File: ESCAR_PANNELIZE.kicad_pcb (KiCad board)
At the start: 2 copper layers, 96.6 x 63.6 mm, 168 parts, among them P1 MICRO_SD, P2 BREADBOARD, P3 PROGRAM, P4 MOTOR_B, P5 MOTOR_A, P6 CONN_01X10, P7 CONN_01X10, P8 POWER_IN, P9 UNIVERSAL_PAD, SW1 RESET, SW2 MULTIFUNCTION_SW, SW3 POWER_SW, U1 ESP-WROOM-02, U2 TC117HS, U3 TC117HS, U4 LD1117CV33

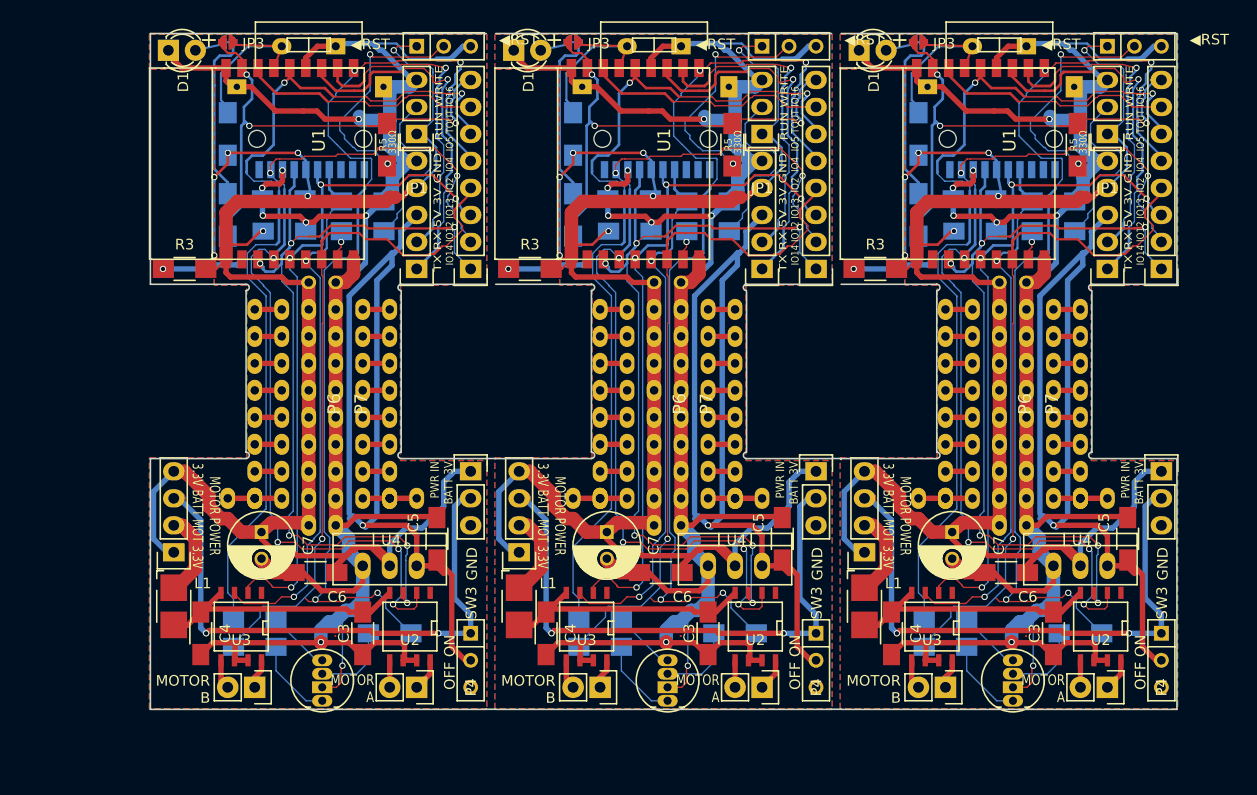
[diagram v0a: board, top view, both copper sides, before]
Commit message: add dividing resisters for RX pin , and organized many point.
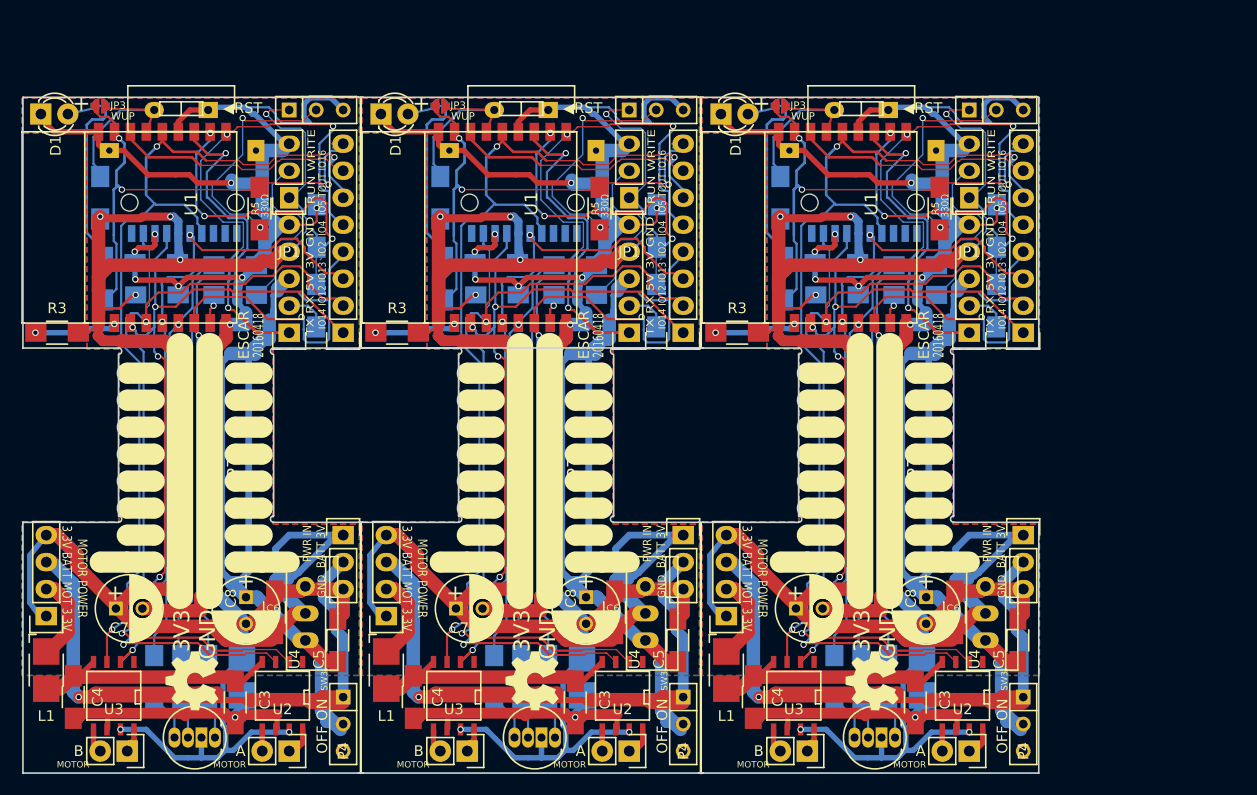
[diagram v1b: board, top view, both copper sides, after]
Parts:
- removed the C1 at (144.5, 67.1)
- removed the C1 at (112.0, 67.1)
- removed the C1 at (177.0, 67.1)
- removed the C2 at (144.5, 70.1)
- removed the C2 at (112.0, 70.1)
- removed the C2 at (177.0, 70.1)
- removed the C3 at (151.9, 108.0)
- removed the C3 at (119.4, 108.0)
- removed the C3 at (184.4, 108.0)
- removed the C4 at (136.6, 108.0)
- removed the C4 at (104.1, 108.0)
- removed the C4 at (169.1, 108.0)
- removed the C5 at (158.9, 99.1)
- removed the C5 at (126.4, 99.1)
- removed the C5 at (191.4, 99.1)
- removed the C6 at (147.4, 102.2)
- removed the C6 at (114.9, 102.2)
- removed the C6 at (179.9, 102.2)
- removed the C7 at (142.4, 98.4)
- removed the C7 at (109.9, 98.4)
- removed the C7 at (174.9, 98.4)
- removed the D1 at (133.6, 53.1)
- removed the D1 at (101.1, 53.1)
- removed the D1 at (166.1, 53.1)
- removed the D2 at (148.1, 114.3)
- removed the D2 at (115.6, 114.3)
- removed the D2 at (180.6, 114.3)
- removed the JP1 at (157.0, 61.0)
- removed the JP1 at (124.5, 61.0)
- removed the JP1 at (189.5, 61.0)
- removed the JP2 at (139.2, 52.3)
- removed the JP2 at (106.7, 52.3)
- removed the JP2 at (171.7, 52.3)
- removed the JP3 at (139.2, 52.3)
- removed the JP3 at (106.7, 52.3)
- removed the JP3 at (171.7, 52.3)
- removed the JP4 at (134.1, 100.3)
- removed the JP4 at (101.6, 100.3)
- removed the JP4 at (166.6, 100.3)
- removed the L1 at (134.1, 105.4)
- removed the L1 at (101.6, 105.4)
- removed the L1 at (166.6, 105.4)
- removed the P1 at (147.4, 58.4)
- removed the P1 at (114.9, 58.4)
- removed the P1 at (179.9, 58.4)
- removed the P2 at (162.0, 73.7)
- removed the P2 at (129.5, 73.7)
- removed the P2 at (194.5, 73.7)
- removed the P3 at (157.0, 73.7)
- removed the P3 at (124.5, 73.7)
- removed the P3 at (189.5, 73.7)
- removed the P4 at (157.0, 113.0)
- removed the P4 at (124.5, 113.0)
- removed the P4 at (189.5, 113.0)
- removed the P5 at (141.7, 113.0)
- removed the P5 at (109.2, 113.0)
- removed the P5 at (174.2, 113.0)
- removed the P6 at (146.8, 86.4)
- removed the P6 at (114.3, 86.4)
- removed the P6 at (179.3, 86.4)
- removed the P7 at (149.3, 86.4)
- removed the P7 at (116.8, 86.4)
- removed the P7 at (181.8, 86.4)
- removed the P8 at (162.0, 92.7)
- removed the P8 at (129.5, 92.7)
- removed the P8 at (194.5, 92.7)
- removed the P9 at (140.4, 95.2)
- removed the P9 at (153.2, 82.5)
- removed the P9 at (143.0, 82.5)
- removed the P9 at (143.0, 85.1)
- removed the P9 at (143.0, 80.0)
- removed the P9 at (143.0, 77.5)
- removed the P9 at (143.0, 87.6)
- removed the P9 at (143.0, 90.2)
- removed the P9 at (143.0, 95.2)
- removed the P9 at (143.0, 92.7)
- removed the P9 at (108.0, 95.2)
- removed the P9 at (155.7, 95.2)
- removed the P9 at (123.2, 95.2)
- removed the P9 at (120.7, 92.7)
- removed the P9 at (120.7, 95.2)
- removed the P9 at (120.7, 90.2)
- removed the P9 at (120.7, 87.6)
- removed the P9 at (120.7, 77.5)
- removed the P9 at (120.7, 80.0)
- removed the P9 at (120.7, 85.1)
- removed the P9 at (120.7, 82.5)
- removed the P9 at (110.5, 82.5)
- removed the P9 at (153.2, 92.7)
- removed the P9 at (110.5, 85.1)
- removed the P9 at (110.5, 80.0)
- removed the P9 at (110.5, 77.5)
- removed the P9 at (110.5, 87.6)
- removed the P9 at (110.5, 90.2)
- removed the P9 at (110.5, 95.2)
- removed the P9 at (110.5, 92.7)
- removed the P9 at (172.9, 95.2)
- removed the P9 at (188.2, 95.2)
- removed the P9 at (185.7, 92.7)
- removed the P9 at (153.2, 95.2)
- removed the P9 at (185.7, 95.2)
- removed the P9 at (185.7, 90.2)
- removed the P9 at (185.7, 87.6)
- removed the P9 at (185.7, 77.5)
- removed the P9 at (185.7, 80.0)
- removed the P9 at (185.7, 85.1)
- removed the P9 at (185.7, 82.5)
- removed the P9 at (175.5, 82.5)
- removed the P9 at (175.5, 85.1)
- removed the P9 at (175.5, 80.0)
- removed the P9 at (153.2, 90.2)
- removed the P9 at (175.5, 77.5)
- removed the P9 at (175.5, 87.6)
- removed the P9 at (175.5, 90.2)
- removed the P9 at (175.5, 95.2)
- removed the P9 at (175.5, 92.7)
- removed the P9 at (153.2, 87.6)
- removed the P9 at (153.2, 77.5)
- removed the P9 at (153.2, 80.0)
- removed the P9 at (153.2, 85.1)
- removed the R1 at (151.9, 67.3)
- removed the R1 at (119.4, 67.3)
- removed the R1 at (184.4, 67.3)
- removed the R2 at (151.9, 70.1)
- removed the R2 at (119.4, 70.1)
- removed the R2 at (184.4, 70.1)
- removed the R3 at (135.1, 73.7)
- removed the R3 at (102.6, 73.7)
- removed the R3 at (167.6, 73.7)
- removed the R4 at (139.2, 61.0)
- removed the R4 at (106.7, 61.0)
- removed the R4 at (171.7, 61.0)
- removed the R5 at (154.2, 62.0)
- removed the R5 at (121.7, 62.0)
- removed the R5 at (186.7, 62.0)
- removed the R6 at (139.2, 68.6)
- removed the R6 at (106.7, 68.6)
- removed the R6 at (171.7, 68.6)
- removed the R7 at (154.4, 108.0)
- removed the R7 at (121.9, 108.0)
- removed the R7 at (186.9, 108.0)
- removed the R8 at (141.7, 106.7)
- removed the R8 at (109.2, 106.7)
- removed the R8 at (174.2, 106.7)
- removed the R9 at (141.7, 109.2)
- removed the R9 at (109.2, 109.2)
- removed the R9 at (174.2, 109.2)
- removed the SW1 at (150.6, 52.6)
- removed the SW1 at (118.1, 52.6)
- removed the SW1 at (183.1, 52.6)
- removed the SW2 at (159.5, 52.7)
- removed the SW2 at (127.0, 52.7)
- removed the SW2 at (192.0, 52.7)
- removed the SW3 at (162.0, 110.5)
- removed the SW3 at (129.5, 110.5)
- removed the SW3 at (194.5, 110.5)
- removed the U1 at (145.0, 63.8)
- removed the U1 at (112.5, 63.8)
- removed the U1 at (177.5, 63.8)
- removed the U2 at (156.3, 107.3)
- removed the U2 at (123.8, 107.3)
- removed the U2 at (188.8, 107.3)
- removed the U3 at (140.4, 107.3)
- removed the U3 at (108.0, 107.3)
- removed the U3 at (172.9, 107.3)
- removed the U4 at (154.4, 101.6)
- removed the U4 at (121.9, 101.6)
- removed the U4 at (186.9, 101.6)
- added C1: 0.1uF, Capacitors_SMD:C_1206_HandSoldering, B.Cu at (100.0, 73.1)
- added C1: 0.1uF, Capacitors_SMD:C_1206_HandSoldering, B.Cu at (132.0, 73.1)
- added C1: 0.1uF, Capacitors_SMD:C_1206_HandSoldering, B.Cu at (164.0, 73.1)
- added C2: 0.1uF, Capacitors_SMD:C_1206_HandSoldering, B.Cu at (100.0, 76.1)
- added C2: 0.1uF, Capacitors_SMD:C_1206_HandSoldering, B.Cu at (132.0, 76.1)
- added C2: 0.1uF, Capacitors_SMD:C_1206_HandSoldering, B.Cu at (164.0, 76.1)
- added C3: 0.1uF, Capacitors_SMD:C_1206_HandSoldering, F.Cu at (107.4, 114.5)
- added C3: 0.1uF, Capacitors_SMD:C_1206_HandSoldering, F.Cu at (139.4, 114.5)
- added C3: 0.1uF, Capacitors_SMD:C_1206_HandSoldering, F.Cu at (171.4, 114.5)
- added C4: 0.1uF, Capacitors_SMD:C_1206_HandSoldering, F.Cu at (92.1, 114.0)
- added C4: 0.1uF, Capacitors_SMD:C_1206_HandSoldering, F.Cu at (124.1, 114.0)
- added C4: 0.1uF, Capacitors_SMD:C_1206_HandSoldering, F.Cu at (156.1, 114.0)
- added C5: 0.1uF, Capacitors_SMD:C_1206_HandSoldering, F.Cu at (117.0, 108.6)
- added C5: 0.1uF, Capacitors_SMD:C_1206_HandSoldering, F.Cu at (149.0, 108.6)
- added C5: 0.1uF, Capacitors_SMD:C_1206_HandSoldering, F.Cu at (181.0, 108.6)
- added C6: 0.1uF, Capacitors_SMD:C_1206_HandSoldering, F.Cu at (111.1, 106.0)
- added C6: 0.1uF, Capacitors_SMD:C_1206_HandSoldering, F.Cu at (143.1, 106.0)
- added C6: 0.1uF, Capacitors_SMD:C_1206_HandSoldering, F.Cu at (175.1, 106.0)
- added C7: 100uF, Capacitors_ThroughHole:C_Radial_D6.3_L11.2_P2.5, F.Cu at (96.2, 105.6)
- added C7: 100uF, Capacitors_ThroughHole:C_Radial_D6.3_L11.2_P2.5, F.Cu at (128.2, 105.6)
- added C7: 100uF, Capacitors_ThroughHole:C_Radial_D6.3_L11.2_P2.5, F.Cu at (160.2, 105.6)
- added C8: 100uF, Capacitors_ThroughHole:C_Radial_D6.3_L11.2_P2.5, F.Cu at (108.4, 104.6)
- added C8: 100uF, Capacitors_ThroughHole:C_Radial_D6.3_L11.2_P2.5, F.Cu at (140.4, 104.6)
- added C8: 100uF, Capacitors_ThroughHole:C_Radial_D6.3_L11.2_P2.5, F.Cu at (172.4, 104.6)
- added D1: YELLOW, LEDs:LED-3MM, F.Cu at (89.1, 59.1)
- added D1: YELLOW, LEDs:LED-3MM, F.Cu at (121.1, 59.1)
- added D1: YELLOW, LEDs:LED-3MM, F.Cu at (153.1, 59.1)
- added D2: LED_RCBG, LEDs:LED-RGB-5MM_Common_Cathode, F.Cu at (105.5, 117.8)
- added D2: LED_RCBG, LEDs:LED-RGB-5MM_Common_Cathode, F.Cu at (137.5, 117.8)
- added D2: LED_RCBG, LEDs:LED-RGB-5MM_Common_Cathode, F.Cu at (169.5, 117.8)
- added JP1: WRITE, Pin_Headers:Pin_Header_Straight_1x03, F.Cu at (112.5, 67.0)
- added JP1: WRITE, Pin_Headers:Pin_Header_Straight_1x03, F.Cu at (144.5, 67.0)
- added JP1: WRITE, Pin_Headers:Pin_Header_Straight_1x03, F.Cu at (176.5, 67.0)
- added JP2: WAKEUP_JUMPER, library:Soldar_Jumper_Unconnected, F.Cu at (94.7, 58.3)
- added JP2: WAKEUP_JUMPER, library:Soldar_Jumper_Unconnected, F.Cu at (126.7, 58.3)
- added JP2: WAKEUP_JUMPER, library:Soldar_Jumper_Unconnected, F.Cu at (158.7, 58.3)
- added JP3: YELLOW_LED, library:Soldar_Jumper_Unconnected, B.Cu at (94.7, 58.3)
- added JP3: YELLOW_LED, library:Soldar_Jumper_Unconnected, B.Cu at (126.7, 58.3)
- added JP3: YELLOW_LED, library:Soldar_Jumper_Unconnected, B.Cu at (158.7, 58.3)
- added JP4: POWER_JUMPER, Pin_Headers:Pin_Header_Straight_1x04, F.Cu at (89.6, 106.3)
- added JP4: POWER_JUMPER, Pin_Headers:Pin_Header_Straight_1x04, F.Cu at (121.6, 106.3)
- added JP4: POWER_JUMPER, Pin_Headers:Pin_Header_Straight_1x04, F.Cu at (153.6, 106.3)
- added L1: INDUCTOR_SMALL, Inductors:Inductor_1212, F.Cu at (89.6, 111.4)
- added L1: INDUCTOR_SMALL, Inductors:Inductor_1212, F.Cu at (121.6, 111.4)
- added L1: INDUCTOR_SMALL, Inductors:Inductor_1212, F.Cu at (153.6, 111.4)
- added L2: INDUCTOR_SMALL, Inductors:Inductor_1212, B.Cu at (108.0, 112.0)
- added L2: INDUCTOR_SMALL, Inductors:Inductor_1212, B.Cu at (140.0, 112.0)
- added L2: INDUCTOR_SMALL, Inductors:Inductor_1212, B.Cu at (172.0, 112.0)
- added OSHW: 1.1, library:OSHW_LOGL_SYLK_5mm, F.Cu at (103.3, 112.4)
- added OSHW: 1.1, library:OSHW_LOGL_SYLK_5mm, F.Cu at (135.3, 112.4)
- added OSHW: 1.1, library:OSHW_LOGL_SYLK_5mm, F.Cu at (167.3, 112.4)
- added P1: MICRO_SD, library:TF_Socket_DONGGUAN_MINYUE_ELECTRONICS, B.Cu at (102.9, 64.4)
- added P1: MICRO_SD, library:TF_Socket_DONGGUAN_MINYUE_ELECTRONICS, B.Cu at (134.9, 64.4)
- added P1: MICRO_SD, library:TF_Socket_DONGGUAN_MINYUE_ELECTRONICS, B.Cu at (166.9, 64.4)
- added P2: BREADBOARD, Pin_Headers:Pin_Header_Straight_1x08, F.Cu at (117.5, 79.7)
- added P2: BREADBOARD, Pin_Headers:Pin_Header_Straight_1x08, F.Cu at (149.5, 79.7)
- added P2: BREADBOARD, Pin_Headers:Pin_Header_Straight_1x08, F.Cu at (181.5, 79.7)
- added P3: PROGRAM, Pin_Headers:Pin_Header_Straight_1x05, F.Cu at (112.5, 79.7)
- added P3: PROGRAM, Pin_Headers:Pin_Header_Straight_1x05, F.Cu at (144.5, 79.7)
- added P3: PROGRAM, Pin_Headers:Pin_Header_Straight_1x05, F.Cu at (176.5, 79.7)
- added P4: MOTOR_A, Pin_Headers:Pin_Header_Straight_1x02, F.Cu at (112.5, 119.0)
- added P4: MOTOR_A, Pin_Headers:Pin_Header_Straight_1x02, F.Cu at (144.5, 119.0)
- added P4: MOTOR_A, Pin_Headers:Pin_Header_Straight_1x02, F.Cu at (176.5, 119.0)
- added P5: MOTOR_B, Pin_Headers:Pin_Header_Straight_1x02, F.Cu at (97.2, 119.0)
- added P5: MOTOR_B, Pin_Headers:Pin_Header_Straight_1x02, F.Cu at (129.2, 119.0)
- added P5: MOTOR_B, Pin_Headers:Pin_Header_Straight_1x02, F.Cu at (161.2, 119.0)
- added P6: CONN_01X10, library:Padmatrix-wide-01x10, F.Cu at (102.3, 92.4)
- added P6: CONN_01X10, library:Padmatrix-wide-01x10, F.Cu at (134.3, 92.4)
- added P6: CONN_01X10, library:Padmatrix-wide-01x10, F.Cu at (166.3, 92.4)
- added P7: CONN_01X10, library:Padmatrix-wide-01x10, F.Cu at (104.8, 92.4)
- added P7: CONN_01X10, library:Padmatrix-wide-01x10, F.Cu at (136.8, 92.4)
- added P7: CONN_01X10, library:Padmatrix-wide-01x10, F.Cu at (168.8, 92.4)
- added P8: POWER_IN, Pin_Headers:Pin_Header_Straight_1x03, F.Cu at (117.5, 98.7)
- added P8: POWER_IN, Pin_Headers:Pin_Header_Straight_1x03, F.Cu at (149.5, 98.7)
- added P8: POWER_IN, Pin_Headers:Pin_Header_Straight_1x03, F.Cu at (181.5, 98.7)
- added P9: UNIVERSAL_PAD, library:Padmatrix-wide-02x01, B.Cu at (96.0, 101.2)
- added P9: UNIVERSAL_PAD, library:Padmatrix-wide-02x01, B.Cu at (108.7, 88.5)
- added P9: UNIVERSAL_PAD, library:Padmatrix-wide-02x01, B.Cu at (98.5, 88.5)
- added P9: UNIVERSAL_PAD, library:Padmatrix-wide-02x01, B.Cu at (98.5, 91.1)
- added P9: UNIVERSAL_PAD, library:Padmatrix-wide-02x01, B.Cu at (98.5, 86.0)
- added P9: UNIVERSAL_PAD, library:Padmatrix-wide-02x01, B.Cu at (98.5, 83.5)
- added P9: UNIVERSAL_PAD, library:Padmatrix-wide-02x01, B.Cu at (98.5, 93.6)
- added P9: UNIVERSAL_PAD, library:Padmatrix-wide-02x01, B.Cu at (98.5, 96.2)
- added P9: UNIVERSAL_PAD, library:Padmatrix-wide-02x01, B.Cu at (98.5, 101.2)
- added P9: UNIVERSAL_PAD, library:Padmatrix-wide-02x01, B.Cu at (98.5, 98.7)
- added P9: UNIVERSAL_PAD, library:Padmatrix-wide-02x01, B.Cu at (128.0, 101.2)
- added P9: UNIVERSAL_PAD, library:Padmatrix-wide-02x01, B.Cu at (111.2, 101.2)
- added P9: UNIVERSAL_PAD, library:Padmatrix-wide-02x01, B.Cu at (143.2, 101.2)
- added P9: UNIVERSAL_PAD, library:Padmatrix-wide-02x01, B.Cu at (140.7, 98.7)
- added P9: UNIVERSAL_PAD, library:Padmatrix-wide-02x01, B.Cu at (140.7, 101.2)
- added P9: UNIVERSAL_PAD, library:Padmatrix-wide-02x01, B.Cu at (140.7, 96.2)
- added P9: UNIVERSAL_PAD, library:Padmatrix-wide-02x01, B.Cu at (140.7, 93.6)
- added P9: UNIVERSAL_PAD, library:Padmatrix-wide-02x01, B.Cu at (140.7, 83.5)
- added P9: UNIVERSAL_PAD, library:Padmatrix-wide-02x01, B.Cu at (140.7, 86.0)
- added P9: UNIVERSAL_PAD, library:Padmatrix-wide-02x01, B.Cu at (140.7, 91.1)
- added P9: UNIVERSAL_PAD, library:Padmatrix-wide-02x01, B.Cu at (140.7, 88.5)
- added P9: UNIVERSAL_PAD, library:Padmatrix-wide-02x01, B.Cu at (130.5, 88.5)
- added P9: UNIVERSAL_PAD, library:Padmatrix-wide-02x01, B.Cu at (108.7, 98.7)
- added P9: UNIVERSAL_PAD, library:Padmatrix-wide-02x01, B.Cu at (130.5, 91.1)
- added P9: UNIVERSAL_PAD, library:Padmatrix-wide-02x01, B.Cu at (130.5, 86.0)
- added P9: UNIVERSAL_PAD, library:Padmatrix-wide-02x01, B.Cu at (130.5, 83.5)
- added P9: UNIVERSAL_PAD, library:Padmatrix-wide-02x01, B.Cu at (130.5, 93.6)
- added P9: UNIVERSAL_PAD, library:Padmatrix-wide-02x01, B.Cu at (130.5, 96.2)
- added P9: UNIVERSAL_PAD, library:Padmatrix-wide-02x01, B.Cu at (130.5, 101.2)
- added P9: UNIVERSAL_PAD, library:Padmatrix-wide-02x01, B.Cu at (130.5, 98.7)
- added P9: UNIVERSAL_PAD, library:Padmatrix-wide-02x01, B.Cu at (159.9, 101.2)
- added P9: UNIVERSAL_PAD, library:Padmatrix-wide-02x01, B.Cu at (175.2, 101.2)
- added P9: UNIVERSAL_PAD, library:Padmatrix-wide-02x01, B.Cu at (172.7, 98.7)
- added P9: UNIVERSAL_PAD, library:Padmatrix-wide-02x01, B.Cu at (108.7, 101.2)
- added P9: UNIVERSAL_PAD, library:Padmatrix-wide-02x01, B.Cu at (172.7, 101.2)
- added P9: UNIVERSAL_PAD, library:Padmatrix-wide-02x01, B.Cu at (172.7, 96.2)
- added P9: UNIVERSAL_PAD, library:Padmatrix-wide-02x01, B.Cu at (172.7, 93.6)
- added P9: UNIVERSAL_PAD, library:Padmatrix-wide-02x01, B.Cu at (172.7, 83.5)
- added P9: UNIVERSAL_PAD, library:Padmatrix-wide-02x01, B.Cu at (172.7, 86.0)
- added P9: UNIVERSAL_PAD, library:Padmatrix-wide-02x01, B.Cu at (172.7, 91.1)
- added P9: UNIVERSAL_PAD, library:Padmatrix-wide-02x01, B.Cu at (172.7, 88.5)
- added P9: UNIVERSAL_PAD, library:Padmatrix-wide-02x01, B.Cu at (162.5, 88.5)
- added P9: UNIVERSAL_PAD, library:Padmatrix-wide-02x01, B.Cu at (162.5, 91.1)
- added P9: UNIVERSAL_PAD, library:Padmatrix-wide-02x01, B.Cu at (162.5, 86.0)
- added P9: UNIVERSAL_PAD, library:Padmatrix-wide-02x01, B.Cu at (108.7, 96.2)
- added P9: UNIVERSAL_PAD, library:Padmatrix-wide-02x01, B.Cu at (162.5, 83.5)
- added P9: UNIVERSAL_PAD, library:Padmatrix-wide-02x01, B.Cu at (162.5, 93.6)
- added P9: UNIVERSAL_PAD, library:Padmatrix-wide-02x01, B.Cu at (162.5, 96.2)
- added P9: UNIVERSAL_PAD, library:Padmatrix-wide-02x01, B.Cu at (162.5, 101.2)
- added P9: UNIVERSAL_PAD, library:Padmatrix-wide-02x01, B.Cu at (162.5, 98.7)
- added P9: UNIVERSAL_PAD, library:Padmatrix-wide-02x01, B.Cu at (108.7, 93.6)
- added P9: UNIVERSAL_PAD, library:Padmatrix-wide-02x01, B.Cu at (108.7, 83.5)
- added P9: UNIVERSAL_PAD, library:Padmatrix-wide-02x01, B.Cu at (108.7, 86.0)
- added P9: UNIVERSAL_PAD, library:Padmatrix-wide-02x01, B.Cu at (108.7, 91.1)
- added R1: 10kΩ, Resistors_SMD:R_1206_HandSoldering, B.Cu at (107.4, 73.3)
- added R1: 10kΩ, Resistors_SMD:R_1206_HandSoldering, B.Cu at (139.4, 73.3)
- added R1: 10kΩ, Resistors_SMD:R_1206_HandSoldering, B.Cu at (171.4, 73.3)
- added R10: 330Ω, Resistors_SMD:R_1206_HandSoldering, B.Cu at (115.1, 69.6)
- added R10: 330Ω, Resistors_SMD:R_1206_HandSoldering, B.Cu at (147.1, 69.6)
- added R10: 330Ω, Resistors_SMD:R_1206_HandSoldering, B.Cu at (179.1, 69.6)
- added R11: 330Ω, Resistors_SMD:R_1206_HandSoldering, B.Cu at (115.0, 77.1)
- added R11: 330Ω, Resistors_SMD:R_1206_HandSoldering, B.Cu at (147.0, 77.1)
- added R11: 330Ω, Resistors_SMD:R_1206_HandSoldering, B.Cu at (179.0, 77.1)
- added R2: 10kΩ, Resistors_SMD:R_1206_HandSoldering, B.Cu at (107.4, 76.1)
- added R2: 10kΩ, Resistors_SMD:R_1206_HandSoldering, B.Cu at (139.4, 76.1)
- added R2: 10kΩ, Resistors_SMD:R_1206_HandSoldering, B.Cu at (171.4, 76.1)
- added R3: 10kΩ, Resistors_SMD:R_1206_HandSoldering, F.Cu at (90.6, 79.7)
- added R3: 10kΩ, Resistors_SMD:R_1206_HandSoldering, F.Cu at (122.6, 79.7)
- added R3: 10kΩ, Resistors_SMD:R_1206_HandSoldering, F.Cu at (154.6, 79.7)
- added R4: 10kΩ, Resistors_SMD:R_1206_HandSoldering, B.Cu at (94.7, 67.0)
- added R4: 10kΩ, Resistors_SMD:R_1206_HandSoldering, B.Cu at (126.7, 67.0)
- added R4: 10kΩ, Resistors_SMD:R_1206_HandSoldering, B.Cu at (158.7, 67.0)
- added R5: 330Ω, Resistors_SMD:R_1206_HandSoldering, F.Cu at (109.7, 68.0)
- added R5: 330Ω, Resistors_SMD:R_1206_HandSoldering, F.Cu at (141.7, 68.0)
- added R5: 330Ω, Resistors_SMD:R_1206_HandSoldering, F.Cu at (173.7, 68.0)
- added R6: 330Ω, Resistors_SMD:R_1206_HandSoldering, B.Cu at (95.0, 74.6)
- added R6: 330Ω, Resistors_SMD:R_1206_HandSoldering, B.Cu at (127.0, 74.6)
- added R6: 330Ω, Resistors_SMD:R_1206_HandSoldering, B.Cu at (159.0, 74.6)
- added R7: 330Ω, Resistors_SMD:R_1206_HandSoldering, B.Cu at (102.3, 112.0)
- added R7: 330Ω, Resistors_SMD:R_1206_HandSoldering, B.Cu at (134.3, 112.0)
- added R7: 330Ω, Resistors_SMD:R_1206_HandSoldering, B.Cu at (166.3, 112.0)
- added R8: 330Ω, Resistors_SMD:R_1206_HandSoldering, B.Cu at (99.8, 112.0)
- added R8: 330Ω, Resistors_SMD:R_1206_HandSoldering, B.Cu at (131.8, 112.0)
- added R8: 330Ω, Resistors_SMD:R_1206_HandSoldering, B.Cu at (163.8, 112.0)
- added R9: 330Ω, Resistors_SMD:R_1206_HandSoldering, B.Cu at (104.8, 112.0)
- added R9: 330Ω, Resistors_SMD:R_1206_HandSoldering, B.Cu at (136.8, 112.0)
- added R9: 330Ω, Resistors_SMD:R_1206_HandSoldering, B.Cu at (168.8, 112.0)
- added SW1: RESET, Buttons_Switches_ThroughHole:SW_DIP_x1_Slide, F.Cu at (106.1, 58.6)
- added SW1: RESET, Buttons_Switches_ThroughHole:SW_DIP_x1_Slide, F.Cu at (138.1, 58.6)
- added SW1: RESET, Buttons_Switches_ThroughHole:SW_DIP_x1_Slide, F.Cu at (170.1, 58.6)
- added SW2: MULTIFUNCTION_SW, Buttons_Switches_ThroughHole:SW_Micro_SPST, F.Cu at (115.0, 58.7)
- added SW2: MULTIFUNCTION_SW, Buttons_Switches_ThroughHole:SW_Micro_SPST, F.Cu at (147.0, 58.7)
- added SW2: MULTIFUNCTION_SW, Buttons_Switches_ThroughHole:SW_Micro_SPST, F.Cu at (179.0, 58.7)
- added SW3: POWER_SW, Buttons_Switches_ThroughHole:SW_Micro_SPST, F.Cu at (117.5, 116.5)
- added SW3: POWER_SW, Buttons_Switches_ThroughHole:SW_Micro_SPST, F.Cu at (149.5, 116.5)
- added SW3: POWER_SW, Buttons_Switches_ThroughHole:SW_Micro_SPST, F.Cu at (181.5, 116.5)
- added U1: ESP-WROOM-02, library:ESP_WROOM_02, F.Cu at (100.5, 69.8)
- added U1: ESP-WROOM-02, library:ESP_WROOM_02, F.Cu at (132.5, 69.8)
- added U1: ESP-WROOM-02, library:ESP_WROOM_02, F.Cu at (164.5, 69.8)
- added U2: TC117HS, SMD_Packages:SOIC-8-N, F.Cu at (111.8, 113.8)
- added U2: TC117HS, SMD_Packages:SOIC-8-N, F.Cu at (143.8, 113.8)
- added U2: TC117HS, SMD_Packages:SOIC-8-N, F.Cu at (175.8, 113.8)
- added U3: TC117HS, SMD_Packages:SOIC-8-N, F.Cu at (96.0, 113.8)
- added U3: TC117HS, SMD_Packages:SOIC-8-N, F.Cu at (128.0, 113.8)
- added U3: TC117HS, SMD_Packages:SOIC-8-N, F.Cu at (159.9, 113.8)
- added U4: LD1117CV33, TO_SOT_Packages_THT:TO-220_Neutral123_Vertical, F.Cu at (114.0, 106.1)
- added U4: LD1117CV33, TO_SOT_Packages_THT:TO-220_Neutral123_Vertical, F.Cu at (146.0, 106.1)
- added U4: LD1117CV33, TO_SOT_Packages_THT:TO-220_Neutral123_Vertical, F.Cu at (178.0, 106.1)
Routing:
- net Net-(P2-Pad6): track 257.5 -> 0.00 mm, vias 6 -> 0
- net Net-(C3-Pad2): track 0.00 -> 133.5 mm, vias 0 -> 3
- net Net-(R1-Pad2): track 0.00 -> 123.7 mm, vias 0 -> 3
- net Net-(R10-Pad2): track 0.00 -> 102.4 mm, vias 0 -> 9
- net +3V3: track 508.6 -> 610.5 mm, vias 21 -> 15
- net Net-(P1-Pad2): track 153.5 -> 253.3 mm, vias 6 -> 9
- net +BATT: track 166.1 -> 258.9 mm, vias 9 -> 6
- net Net-(P3-Pad2): track 93.2 -> 14.7 mm, vias 3 -> 0
- net Net-(P2-Pad5): track 283.1 -> 238.2 mm, vias 12 -> 6
- net Net-(P1-Pad7): track 271.2 -> 255.3 mm, vias 18 -> 6
- net +5V: track 258.8 -> 271.6 mm, vias 3 -> 0
- net Net-(D2-Pad1): track 23.3 -> 11.9 mm
- net Net-(D2-Pad3): track 24.0 -> 13.8 mm
- net Net-(P2-Pad4): track 195.0 -> 185.6 mm, vias 3 -> 6
- net GND: track 586.1 -> 578.7 mm, vias 24 -> 30
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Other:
- board size 96.6 x 63.6 mm -> 95.6 x 63.6 mm
- board text added: "20160418"
- board text added: "3V3 GND"
- board text added: "A"
- board text added: "B"
- board text added: "ESCAR"
- board text added: "GND IO16 3.3V"
- board text added: "MOTOR"
- board text added: "Micro_SD:CS=IO5"
- board text added: "WUP"
- board text added: "YELLOW_LED"
- board text removed: "MOTOR A"
- board text removed: "MOTOR B"
